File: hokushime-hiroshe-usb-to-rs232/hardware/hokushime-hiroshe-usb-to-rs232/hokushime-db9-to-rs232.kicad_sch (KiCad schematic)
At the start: 37 parts, among them IC1 SP3243EC/EB, J1 Conn1, J2 USB_B, J3 Conn2, U1 FT232BM/BL, U3 93CxxC, Y1 6Mhz

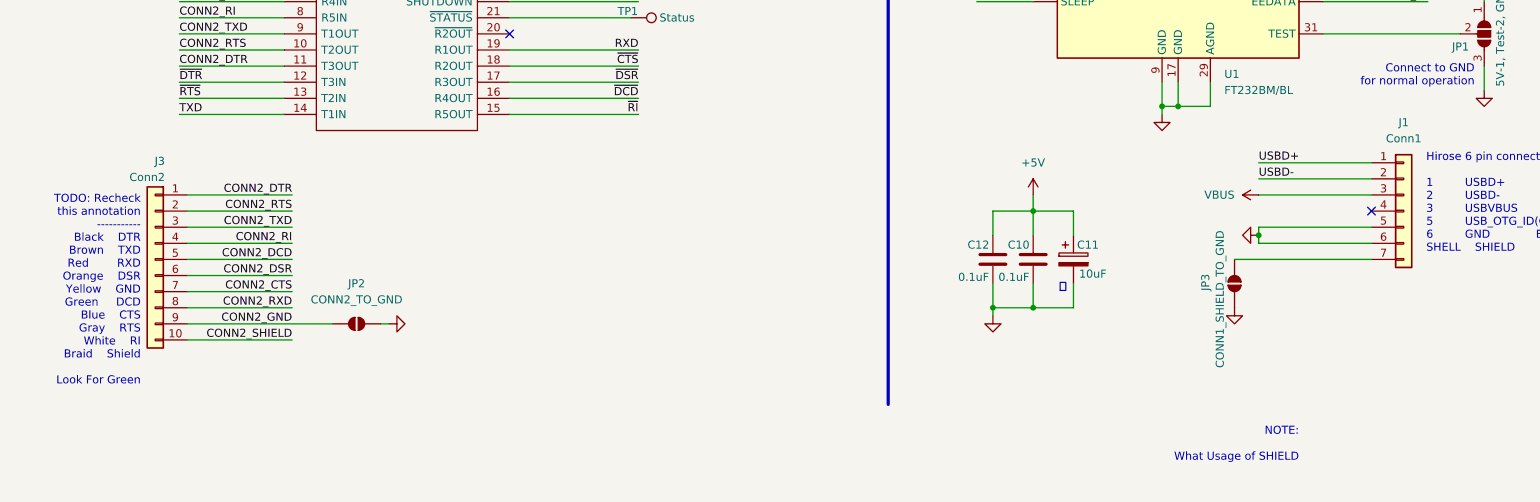
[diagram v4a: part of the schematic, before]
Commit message: [05-18-0917] re-routing and flip component
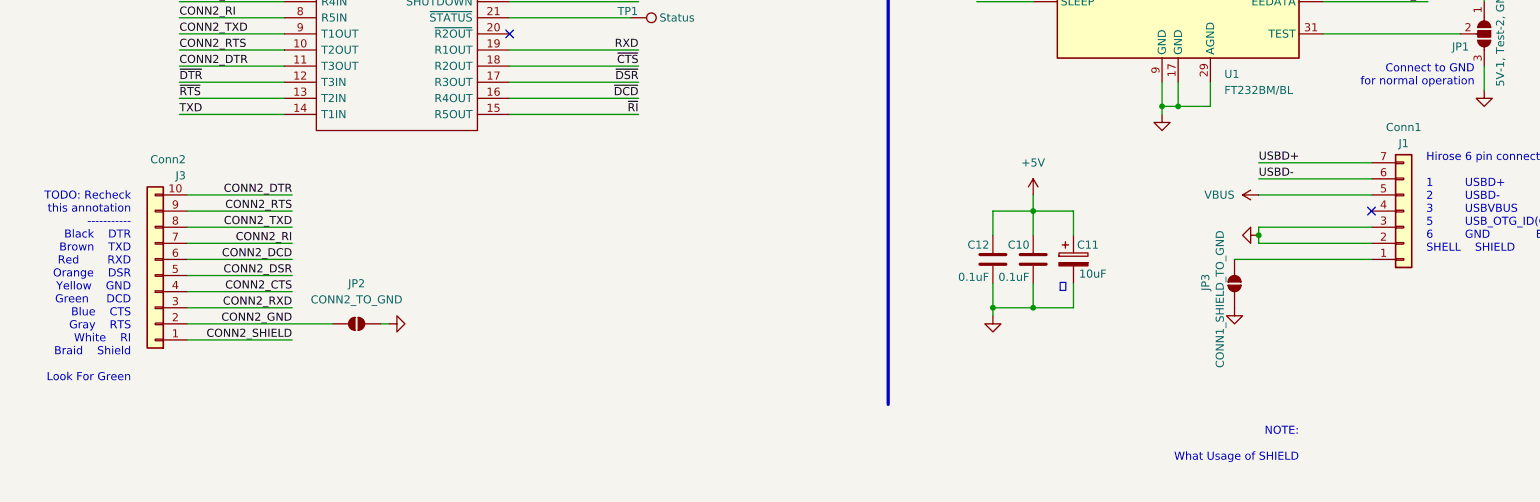
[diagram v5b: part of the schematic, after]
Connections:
- net CONN2_CTS: now also J3.4 (Pin_4); no longer J3.7 (Pin_7)
- net CONN2_DCD: now also J3.6 (Pin_6); no longer J3.5 (Pin_5)
- net CONN2_DSR: now also J3.5 (Pin_5); no longer J3.6 (Pin_6)
- net CONN2_DTR: now also J3.10 (Pin_10); no longer J3.1 (Pin_1)
- net CONN2_GND: now also J3.2 (Pin_2); no longer J3.9 (Pin_9)
- net CONN2_RI: now also J3.7 (Pin_7); no longer J3.4 (Pin_4)
- net CONN2_RTS: now also J3.9 (Pin_9); no longer J3.2 (Pin_2)
- net CONN2_RXD: now also J3.3 (Pin_3); no longer J3.8 (Pin_8)
- net CONN2_SHIELD: now also J3.1 (Pin_1); no longer J3.10 (Pin_10)
- net CONN2_TXD: now also J3.8 (Pin_8); no longer J3.3 (Pin_3)
- net GND: now also J1.2 (Pin_2), J1.3 (Pin_3); no longer J1.5 (Pin_5), J1.6 (Pin_6)
- net USBD+: now also J1.7 (Pin_7); no longer J1.1 (Pin_1)
- net USBD-: now also J1.6 (Pin_6); no longer J1.2 (Pin_2)
- net VBUS: now also J1.5 (Pin_5); no longer J1.3 (Pin_3)
- net at JP3.2 (B): now also J1.1 (Pin_1); no longer J1.7 (Pin_7)
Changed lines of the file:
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@@
 	(text "TODO: Recheck \nthis annotation\n-----------\nBlack	DTR\nBrown	TXD\nRed		RXD\nOrange	DSR\nYellow	GND\nGreen 	DCD\nBlue	CTS\nGray	RTS\nWhite	RI\nBraid	Shield\n\nLook For Green "
 		(exclude_from_sim no)
-		(at 29.464 121.92 0)
+		(at 27.94 121.412 0)
 		(effects
 			(font
@@
 	)
 	(symbol
-		(lib_id "Connector_Generic:Conn_01x07")
-		(at 228.6 124.46 0)
-		(unit 1)
-		(exclude_from_sim no)
-		(in_bom yes)
-		(on_board yes)
-		(dnp no)
-		(property "Reference" "J1"
-			(at 228.6 110.49 0)
-			(effects
-				(font
-					(size 1.27 1.27)
-				)
-			)
-		)
-		(property "Value" "Conn1"
-			(at 228.6 113.03 0)
-			(effects
-				(font
-					(size 1.27 1.27)
-				)
-			)
-		)
-		(property "Footprint" "Connector_PinHeader_2.54mm:PinHeader_1x07_P2.54mm_Horizontal"
-			(at 228.6 124.46 0)
-			(effects
-				(font
-					(size 1.27 1.27)
-				)
-				(hide yes)
-			)
-		)
-		(property "Datasheet" "~"
-			(at 228.6 124.46 0)
-			(effects
-				(font
-					(size 1.27 1.27)
-				)
-				(hide yes)
-			)
-		)
-		(property "Description" "Generic connector, single row, 01x07, script generated (kicad-library-utils/schlib/autogen/connector/)"
-			(at 228.6 124.46 0)
-			(effects
-				(font
-					(size 1.27 1.27)
-				)
-				(hide yes)
-			)
-		)
-		(pin "4"
-		)
-		(pin "1"
-		)
-		(pin "5"
-		)
-		(pin "6"
-		)
-		(pin "3"
-		)
-		(pin "7"
-		)
-		(pin "2"
-		)
-		(instances
-			(project "hokushime-db9-to-rs232"
-				(path "/7534cebe-c86f-414b-a564-4eccbebe3bbc"
-					(reference "J1")
-					(unit 1)
-				)
-			)
-		)
-	)
-	(symbol
 		(lib_id "Mechanical:MountingHole")
 		(at 271.78 179.07 0)
@@
 	)
 	(symbol
-		(lib_id "Connector_Generic:Conn_01x10")
-		(at 31.75 132.08 0)
-		(mirror y)
-		(unit 1)
-		(exclude_from_sim no)
-		(in_bom yes)
-		(on_board yes)
-		(dnp no)
-		(property "Reference" "J3"
-			(at 33.274 116.586 0)
-			(effects
-				(font
-					(size 1.27 1.27)
-				)
-				(justify left)
-			)
-		)
-		(property "Value" "Conn2"
-			(at 33.274 119.126 0)
-			(effects
-				(font
-					(size 1.27 1.27)
-				)
-				(justify left)
-			)
-		)
-		(property "Footprint" "Connector_PinHeader_2.54mm:PinHeader_1x10_P2.54mm_Horizontal"
-			(at 31.75 132.08 0)
-			(effects
-				(font
-					(size 1.27 1.27)
-				)
-				(hide yes)
-			)
-		)
-		(property "Datasheet" "~"
-			(at 31.75 132.08 0)
-			(effects
-				(font
-					(size 1.27 1.27)
-				)
-				(hide yes)
-			)
-		)
-		(property "Description" "Generic connector, single row, 01x10, script generated (kicad-library-utils/schlib/autogen/connector/)"
-			(at 31.75 132.08 0)
-			(effects
-				(font
-					(size 1.27 1.27)
-				)
-				(hide yes)
-			)
-		)
-		(pin "2"
-		)
-		(pin "8"
-		)
-		(pin "3"
-		)
-		(pin "6"
-		)
-		(pin "9"
-		)
-		(pin "1"
-		)
-		(pin "4"
-		)
-		(pin "10"
-		)
-		(pin "5"
-		)
-		(pin "7"
-		)
-		(instances
-			(project "hokushime-db9-to-rs232"
-				(path "/7534cebe-c86f-414b-a564-4eccbebe3bbc"
-					(reference "J3")
-					(unit 1)
-				)
-			)
-		)
-	)
-	(symbol
 		(lib_id "Mechanical:MountingHole")
 		(at 276.86 179.07 0)
@@
 	)
 	(symbol
+		(lib_id "Connector_Generic:Conn_01x10")
+		(at 31.75 134.62 180)
+		(unit 1)
+		(exclude_from_sim no)
+		(in_bom yes)
+		(on_board yes)
+		(dnp no)
+		(property "Reference" "J3"
+			(at 36.576 118.872 0)
+			(effects
+				(font
+					(size 1.27 1.27)
+				)
+				(justify left)
+			)
+		)
+		(property "Value" "Conn2"
+			(at 36.576 116.332 0)
+			(effects
+				(font
+					(size 1.27 1.27)
+				)
+				(justify left)
+			)
+		)
+		(property "Footprint" "Connector_PinHeader_2.54mm:PinHeader_1x10_P2.54mm_Horizontal"
+			(at 31.75 134.62 0)
+			(effects
+				(font
+					(size 1.27 1.27)
+				)
+				(hide yes)
+			)
+		)
+		(property "Datasheet" "~"
+			(at 31.75 134.62 0)
+			(effects
+				(font
+					(size 1.27 1.27)
+				)
+				(hide yes)
+			)
+		)
+		(property "Description" "Generic connector, single row, 01x10, script generated (kicad-library-utils/schlib/autogen/connector/)"
+			(at 31.75 134.62 0)
+			(effects
+				(font
+					(size 1.27 1.27)
+				)
+				(hide yes)
+			)
+		)
+		(pin "2"
+		)
+		(pin "8"
+		)
+		(pin "3"
+		)
+		(pin "6"
+		)
+		(pin "9"
+		)
+		(pin "1"
+		)
+		(pin "4"
+		)
+		(pin "10"
+		)
+		(pin "5"
+		)
+		(pin "7"
+		)
+		(instances
+			(project "hokushime-db9-to-rs232"
+				(path "/7534cebe-c86f-414b-a564-4eccbebe3bbc"
+					(reference "J3")
+					(unit 1)
+				)
+			)
+		)
+	)
+	(symbol
 		(lib_id "Device:C")
 		(at 170.18 132.08 180)
@@
 					(unit 1)
 				)
+			)
+		)
+	)
+	(symbol
+		(lib_id "Connector_Generic:Conn_01x07")
+		(at 228.6 124.46 0)
+		(mirror x)
+		(unit 1)
+		(exclude_from_sim no)
+		(in_bom yes)
+		(on_board yes)
+		(dnp no)
+		(property "Reference" "J1"
+			(at 228.6 113.792 0)
+			(effects
+				(font
+					(size 1.27 1.27)
+				)
+			)
+		)
+		(property "Value" "Conn1"
+			(at 228.6 111.252 0)
+			(effects
+				(font
+					(size 1.27 1.27)
+				)
+			)
+		)
+		(property "Footprint" "Connector_PinHeader_2.54mm:PinHeader_1x07_P2.54mm_Horizontal"
+			(at 228.6 124.46 0)
+			(effects
+				(font
+					(size 1.27 1.27)
+				)
+				(hide yes)
+			)
+		)
+		(property "Datasheet" "~"
+			(at 228.6 124.46 0)
+			(effects
+				(font
+					(size 1.27 1.27)
+				)
+				(hide yes)
+			)
+		)
+		(property "Description" "Generic connector, single row, 01x07, script generated (kicad-library-utils/schlib/autogen/connector/)"
+			(at 228.6 124.46 0)
+			(effects
+				(font
+					(size 1.27 1.27)
+				)
+				(hide yes)
+			)
+		)
+		(pin "4"
+		)
+		(pin "1"
+		)
+		(pin "5"
+		)
+		(pin "6"
+		)
+		(pin "3"
+		)
+		(pin "7"
+		)
+		(pin "2"
+		)
+		(instances
+			(project "hokushime-db9-to-rs232"
+				(path "/7534cebe-c86f-414b-a564-4eccbebe3bbc"
+					(reference "J1")
+					(unit 1)
+				)

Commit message: [06-13-0759] change package to correct package SSOP and 32QFP, also make manufacture step doc
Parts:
- IC1: footprint Package_SO:TSSOP-28_4.4x9.7mm_P0.65mm -> Package_SO:SSOP-28_5.3x10.2mm_P0.65mm
- U1: footprint Package_QFP:LQFP-48_7x7mm_P0.5mm -> Package_QFP:LQFP-32_7x7mm_P0.8mm
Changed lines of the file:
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@@
 			)
 		)
-		(property "Footprint" "Package_SO:TSSOP-28_4.4x9.7mm_P0.65mm"
+		(property "Footprint" "Package_SO:SSOP-28_5.3x10.2mm_P0.65mm"
 			(at 83.82 73.66 0)
 			(effects
@@
 			)
 		)
-		(property "Footprint" "Package_QFP:LQFP-48_7x7mm_P0.5mm"
+		(property "Footprint" "Package_QFP:LQFP-32_7x7mm_P0.8mm"
 			(at 218.44 101.6 0)
 			(effects
